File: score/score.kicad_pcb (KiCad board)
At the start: 2 copper layers, 62 x 46 mm, 23 parts, among them J1 Conn_01x02, P8 CONN_01X07, P9 CONN_01X07, U1 74HC595T16-13, U2 HDSP-C8A1, U3 HDSP-C8A1, U4 HDSP-C8A1, U5 74HC595T16-13, U6 74HC595T16-13, U7 TSR1-2433

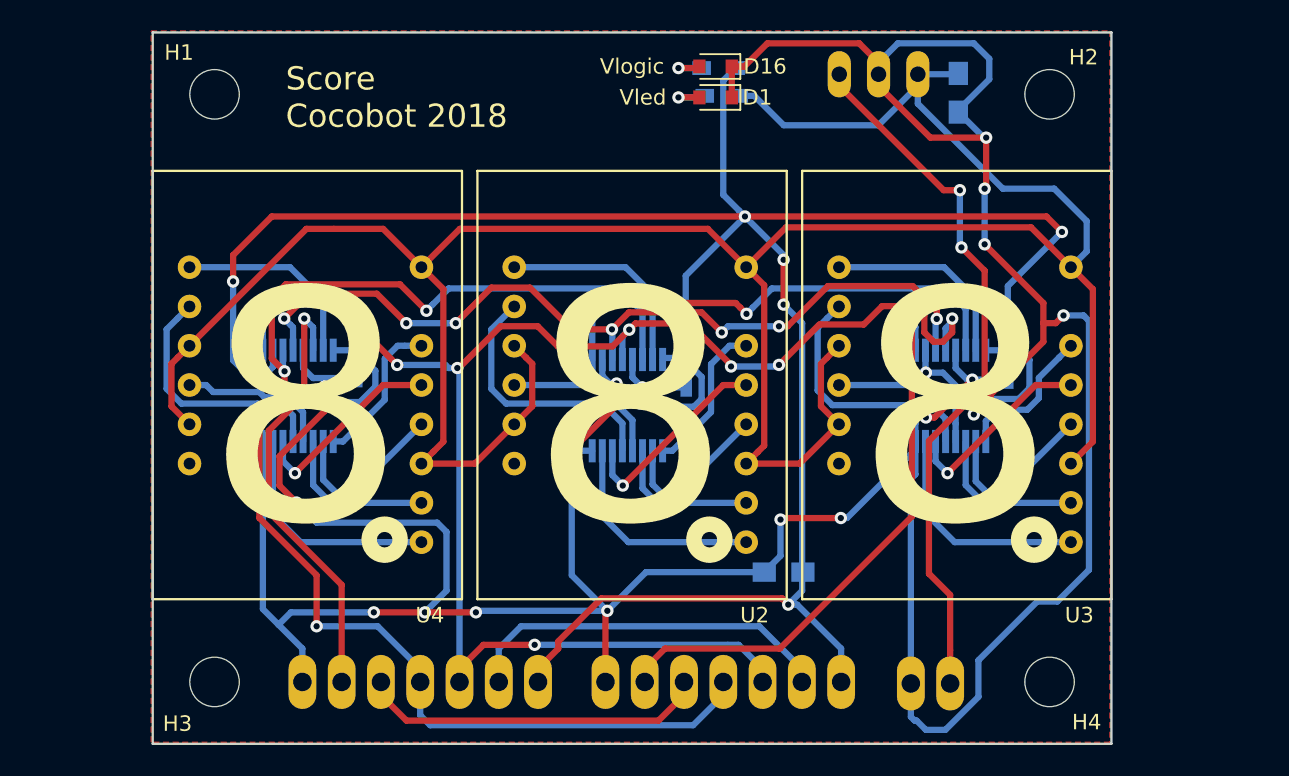
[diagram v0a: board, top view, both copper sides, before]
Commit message: resistor added on 7-seg
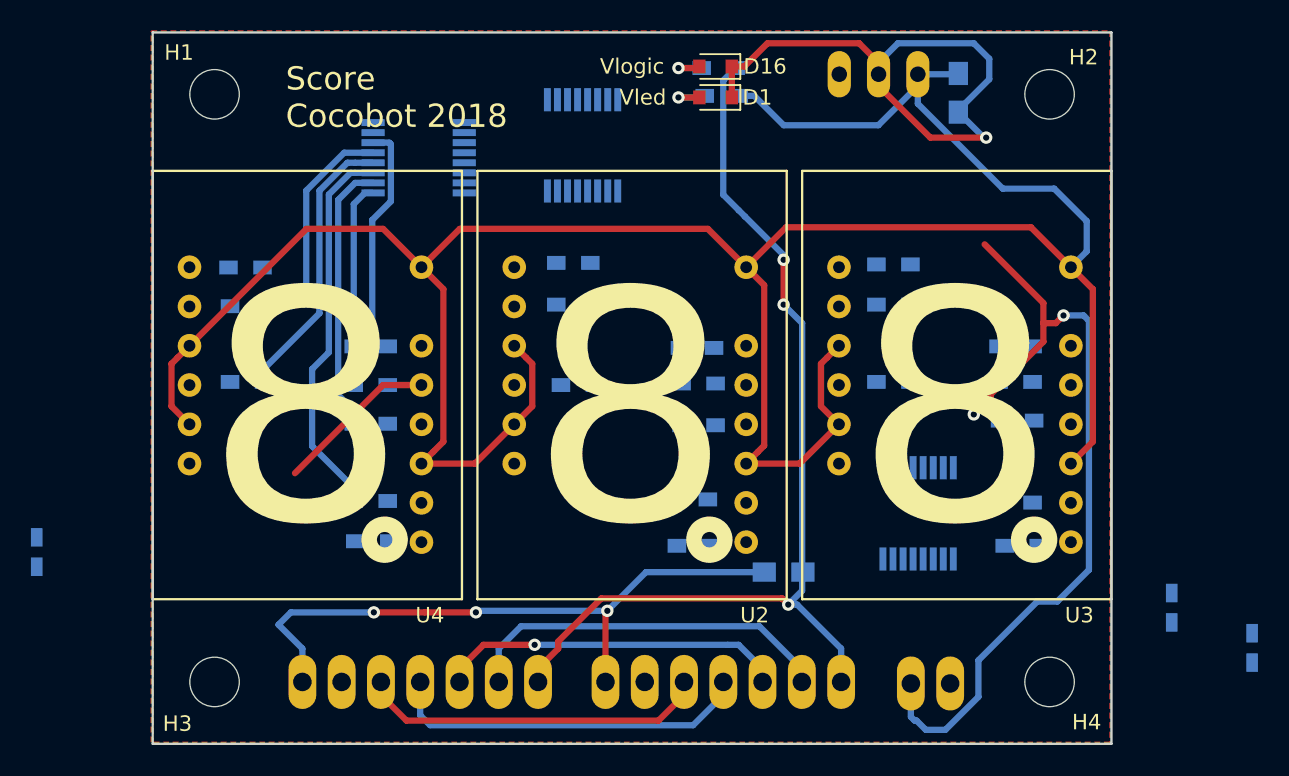
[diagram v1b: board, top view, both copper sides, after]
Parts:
- added R10: 220, espitall:R_0603_HandSoldering, B.Cu at (56.1, 67.7)
- added R11: 220, espitall:R_0603_HandSoldering, B.Cu at (85.2, 70.4)
- added R12: 220, espitall:R_0603_HandSoldering, B.Cu at (77.2, 67.6)
- added R13: 220, espitall:R_0603_HandSoldering, B.Cu at (105.8, 70.3)
- added R14: 220, espitall:R_0603_HandSoldering, B.Cu at (97.9, 67.6)
- added R15: 220, espitall:R_0603_HandSoldering, B.Cu at (85.3, 75.4)
- added R16: 220, espitall:R_0603_HandSoldering, B.Cu at (85.3, 72.7)
- added R17: 220, espitall:R_0603_HandSoldering, B.Cu at (64.1, 75.3)
- added R18: 220, espitall:R_0603_HandSoldering, B.Cu at (64.1, 72.8)
- added R19: 220, espitall:R_0603_HandSoldering, B.Cu at (105.9, 75.1)
- added R20: 220, espitall:R_0603_HandSoldering, B.Cu at (105.8, 72.6)
- added R21: 220, espitall:R_0603_HandSoldering, B.Cu at (84.8, 80.2)
- added R22: 220, espitall:R_0603_HandSoldering, B.Cu at (85.0, 83.2)
- added R23: 220, espitall:R_0603_HandSoldering, B.Cu at (64.1, 80.3)
- added R24: 220, espitall:R_0603_HandSoldering, B.Cu at (64.2, 82.9)
- added R25: 220, espitall:R_0603_HandSoldering, B.Cu at (105.8, 80.4)
- added R26: 220, espitall:R_0603_HandSoldering, B.Cu at (106.2, 83.2)
- added R3: 220, espitall:R_0603_HandSoldering, B.Cu at (56.0, 65.2)
- added R4: 220, espitall:R_0603_HandSoldering, B.Cu at (56.1, 72.6)
- added R5: 220, espitall:R_0603_HandSoldering, B.Cu at (77.2, 64.9)
- added R6: 220, espitall:R_0603_HandSoldering, B.Cu at (77.5, 72.8)
- added R7: 220, espitall:R_0603_HandSoldering, B.Cu at (97.9, 65.0)
- added R8: 220, espitall:R_0603_HandSoldering, B.Cu at (97.9, 72.6)
- added R9: 220, espitall:R_0603_HandSoldering, B.Cu at (64.1, 70.3)
- moved C3 34.9 mm to (115.9, 87.2)
- moved C4 24.2 mm to (121.1, 89.8)
- moved C2 24.0 mm to (42.5, 83.6)
- moved U1 17.3 mm to (67.2, 58.1), turned to 0 degrees
- moved U5 17.0 mm to (77.8, 57.3)
- moved U6 7.88 mm to (99.5, 81.1), turned to 270 degrees
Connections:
- U2 pad 1: /ch8_3v3 -> Net-(R5-Pad1)
- U2 pad 10: /ch11_3v3 -> Net-(R21-Pad1)
- U2 pad 12: /ch10_3v3 -> Net-(R15-Pad1)
- U2 pad 13: /ch14_3v3 -> Net-(R16-Pad1)
- U2 pad 14: /ch9_3v3 -> Net-(R11-Pad1)
- U2 pad 2: /ch13_3v3 -> Net-(R12-Pad1)
- U2 pad 4: /ch12_3v3 -> Net-(R6-Pad1)
- U2 pad 9: /ch15_3v3 -> Net-(R22-Pad1)
- U3 pad 1: /ch16_3v3 -> Net-(R7-Pad1)
- U3 pad 10: /ch19_3v3 -> Net-(R25-Pad1)
- U3 pad 12: /ch18_3v3 -> Net-(R19-Pad1)
- U3 pad 13: /ch22_3v3 -> Net-(R20-Pad1)
- U3 pad 14: /ch17_3v3 -> Net-(R13-Pad1)
- U3 pad 2: /ch21_3v3 -> Net-(R14-Pad1)
- U3 pad 4: /ch20_3v3 -> Net-(R8-Pad1)
- U3 pad 9: /ch23_3v3 -> Net-(R26-Pad1)
- U4 pad 1: /ch0_3v3 -> Net-(R3-Pad1)
- U4 pad 10: /ch3_3v3 -> Net-(R23-Pad1)
- U4 pad 12: /ch2_3v3 -> Net-(R17-Pad1)
- U4 pad 13: /ch6_3v3 -> Net-(R18-Pad1)
- U4 pad 14: /ch1_3v3 -> Net-(R9-Pad1)
- U4 pad 2: /ch5_3v3 -> Net-(R10-Pad1)
- U4 pad 4: /ch4_3v3 -> Net-(R4-Pad1)
- U4 pad 9: /ch7_3v3 -> Net-(R24-Pad1)
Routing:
- net +3V3: track 192.8 -> 66.1 mm, vias 8 -> 3
- net GND: track 249.1 -> 133.4 mm, vias 17 -> 6
- net /sck_3v3: track 110.4 -> 23.7 mm, vias 8 -> 0
- net /set_output_3v3: track 102.8 -> 22.6 mm, vias 8 -> 1
- net Net-(J1-Pad1): track 46.0 -> 0.00 mm, vias 2 -> 0
- net Net-(P9-Pad6): track 36.5 -> 0.00 mm, vias 1 -> 0
- net Net-(U1-Pad9): track 33.1 -> 0.00 mm, vias 2 -> 0
- net Net-(U5-Pad9): track 31.6 -> 0.00 mm, vias 2 -> 0
- net /mosi_3v3: track 28.7 -> 0.00 mm, vias 1 -> 0
- net /ch13_3v3: track 17.1 -> 0.00 mm
- net /ch21_3v3: track 16.5 -> 0.00 mm
- net /ch7_3v3: track 15.1 -> 0.00 mm
- net /ch23_3v3: track 14.8 -> 0.00 mm
- net /ch3_3v3: track 10.3 -> 24.8 mm
- net /ch15_3v3: track 14.2 -> 0.00 mm
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
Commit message: score board routed
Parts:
- moved C3 39.1 mm to (86.9, 61.0)
- moved C2 32.4 mm to (65.3, 60.6)
- moved C4 31.7 mm to (106.8, 61.5)
- moved U6 17.5 mm to (101.7, 63.8), turned to 90 degrees
- moved U1 8.47 mm to (60.2, 62.9), turned to 90 degrees
- moved U5 6.95 mm to (81.8, 63.0)
- moved R1 5.91 mm to (80.7, 52.3), turned to 0 degrees
- moved C1 5.88 mm to (96.0, 87.6), turned to 0 degrees
- moved R3 3.71 mm to (53.5, 62.5)
- moved R7 3.39 mm to (95.4, 62.7)
- moved R5 3.34 mm to (74.5, 62.9)
- moved R14 2.74 mm to (98.7, 70.2)
- moved R12 2.68 mm to (77.7, 70.2)
- moved R10 2.53 mm to (56.9, 70.1)
- moved R8 0.80 mm to (98.7, 72.8)
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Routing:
- net /sck_3v3: track 23.7 -> 120.8 mm, vias 0 -> 6
- net /set_output_3v3: track 22.6 -> 114.9 mm, vias 1 -> 7
- net +3V3: track 66.1 -> 136.3 mm, vias 3 -> 8
- net Net-(P9-Pad6): track 0.00 -> 51.3 mm
- net Net-(J1-Pad1): track 0.00 -> 48.5 mm, vias 0 -> 1
- net /mosi_3v3: track 0.00 -> 47.3 mm
- net Net-(U1-Pad9): track 0.00 -> 30.6 mm, vias 0 -> 2
- net GND: track 133.4 -> 105.1 mm, vias 6 -> 10
- net Net-(U5-Pad9): track 0.00 -> 27.4 mm, vias 0 -> 2
- net /ch19_3v3: track 0.00 -> 26.1 mm
- net /ch15_3v3: track 0.00 -> 24.7 mm
- net /ch7_3v3: track 0.00 -> 22.0 mm
- net /ch23_3v3: track 0.00 -> 22.0 mm
- net /ch22_3v3: track 0.00 -> 19.8 mm
- net +3.3VP: track 175.2 -> 157.2 mm
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
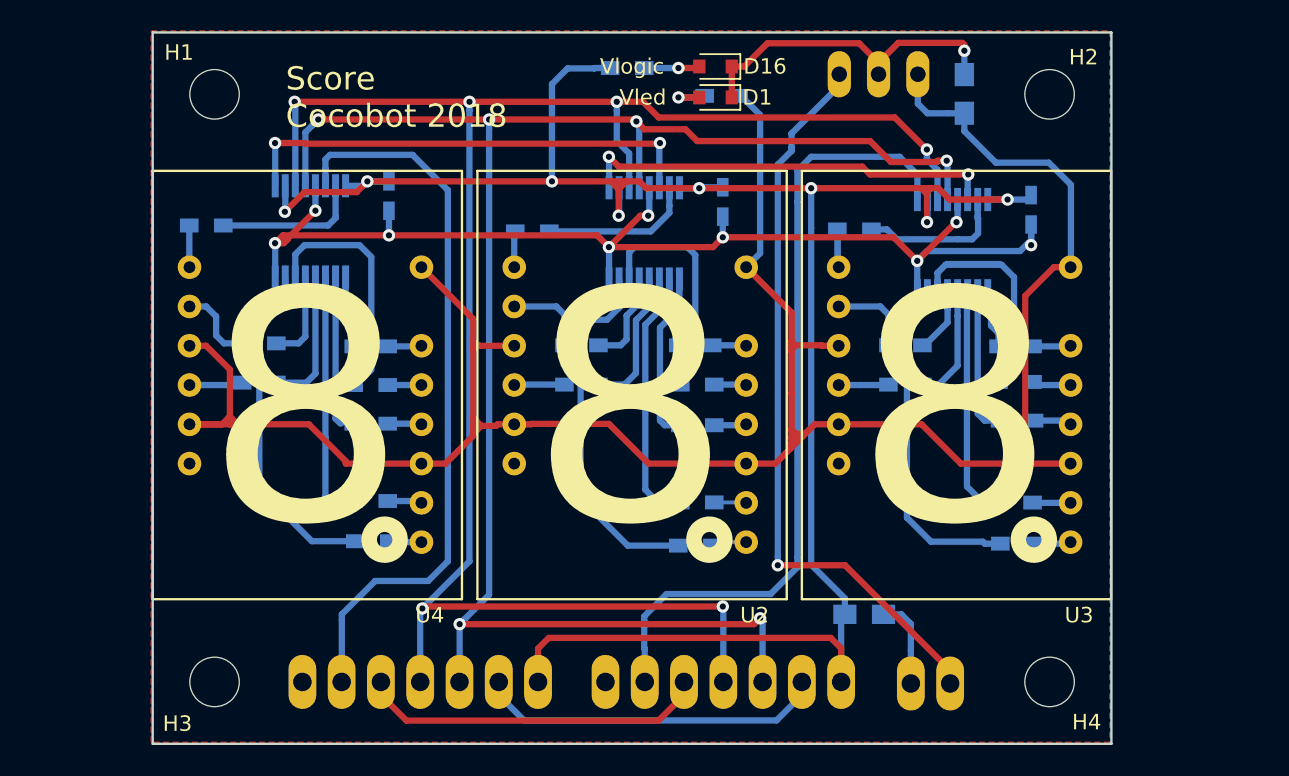
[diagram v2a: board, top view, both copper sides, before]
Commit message: rerouting for non metalized holes
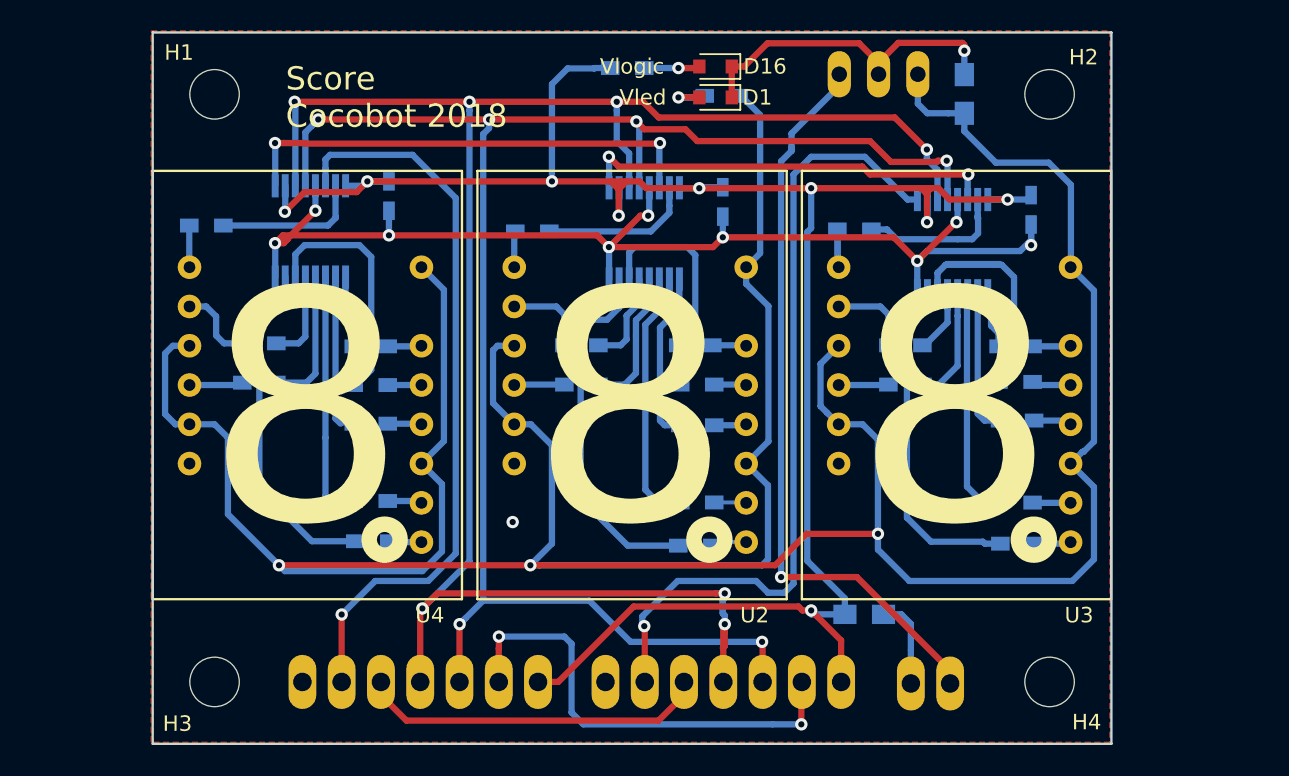
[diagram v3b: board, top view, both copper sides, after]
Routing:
- net +3.3VP: track 157.2 -> 229.8 mm, vias 0 -> 3
- net /load_input_3v3: track 22.7 -> 31.9 mm, vias 0 -> 2
- net /sck_3v3: track 120.8 -> 125.1 mm, vias 6 -> 7
- net /set_output_3v3: track 114.9 -> 112.8 mm
- net /mosi_3v3: track 47.3 -> 48.6 mm, vias 0 -> 1
- net +3V3: track 136.3 -> 135.5 mm, vias 8 -> 9
- net Net-(P9-Pad6): track 51.3 -> 51.8 mm, vias 0 -> 1
- net GND: vias 10 -> 11

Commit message: rerouting for non metalized holes...2
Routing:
- net GND: track 105.1 -> 115.2 mm, vias 11 -> 14
- net Net-(J1-Pad1): track 48.6 -> 50.6 mm
- net +3V3: track 135.5 -> 137.2 mm
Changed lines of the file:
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@@
     (thickness 1.6)
     (drawings 11)
-    (tracks 593)
+    (tracks 602)
     (zones 0)
     (modules 47)
@@
   (page A4)
   (layers
-    (0 F.Cu signal)
+    (0 F.Cu signal hide)
     (31 B.Cu signal)
     (32 B.Adhes user)
@@
   )
   (setup
-    (last_trace_width 0.4064)
+    (last_trace_width 0.25)
     (user_trace_width 0.254)
     (user_trace_width 0.4064)
@@
   (gr_line (start 50 96) (end 112 96) (layer Edge.Cuts) (width 0.15))
   (gr_line (start 50 50) (end 112 50) (layer Edge.Cuts) (width 0.15))
-  (segment (start 76.22683 92) (end 81.10483 87.122) (width 0.4064) (layer F.Cu) (net 1))
-  (segment (start 74.92 92) (end 76.22683 92) (width 0.4064) (layer F.Cu) (net 1))
-  (segment (start 81.10483 87.122) (end 91.763315 87.122) (width 0.4064) (layer F.Cu) (net 1))
+  (segment (start 74.92 89.164) (end 76.962 87.122) (width 0.4064) (layer F.Cu) (net 1))
+  (segment (start 74.92 92) (end 74.92 89.164) (width 0.4064) (layer F.Cu) (net 1))
+  (segment (start 76.962 87.122) (end 91.763315 87.122) (width 0.4064) (layer F.Cu) (net 1))
   (segment (start 91.763315 87.122) (end 92.017315 87.376) (width 0.4064) (layer F.Cu) (net 1))
   (segment (start 92.017315 87.376) (end 92.583 87.376) (width 0.4064) (layer F.Cu) (net 1))
@@
   (segment (start 58.573 59.915) (end 58.573 61.569) (width 0.4064) (layer B.Cu) (net 1))
   (via (at 58.547 61.595) (size 0.8) (drill 0.4) (layers F.Cu B.Cu) (net 1))
+  (via (at 59.68 88.402) (size 0.8) (drill 0.4) (layers F.Cu B.Cu) (net 2))
+  (segment (start 59.68 92) (end 59.68 88.402) (width 0.25) (layer F.Cu) (net 2))
+  (via (at 79.28 89.313) (size 0.8) (drill 0.4) (layers F.Cu B.Cu) (net 2))
+  (segment (start 79.28 92) (end 79.28 89.313) (width 0.25) (layer F.Cu) (net 2))
+  (segment (start 99.06 88.2716) (end 99.03 88.2416) (width 0.25) (layer F.Cu) (net 2))
+  (segment (start 99.06 90.06994) (end 99.06 88.2716) (width 0.25) (layer F.Cu) (net 2))
+  (via (at 99.03 88.2416) (size 0.8) (drill 0.4) (layers F.Cu B.Cu) (net 2))
+  (segment (start 99.03 92.1) (end 99.03 90.09994) (width 0.25) (layer F.Cu) (net 2))
+  (segment (start 99.03 90.09994) (end 99.06 90.06994) (width 0.25) (layer F.Cu) (net 2))
   (via (at 73.279 81.661) (size 0.8) (drill 0.4) (layers F.Cu B.Cu) (net 2))
   (segment (start 97.262 87.63) (end 98.4184 87.63) (width 0.4064) (layer B.Cu) (net 2))
@@
   (segment (start 104.700001 70.3) (end 104.700001 69.4436) (width 0.4064) (layer B.Cu) (net 37))
   (segment (start 104.700001 69.4436) (end 104.217401 68.961) (width 0.4064) (layer B.Cu) (net 37))
-  (segment (start 101.57 91.25037) (end 95.53663 85.217) (width 0.4064) (layer F.Cu) (net 38))
+  (segment (start 101.57 87.854) (end 98.933 85.217) (width 0.4064) (layer F.Cu) (net 38))
+  (segment (start 101.57 92.1) (end 101.57 87.854) (width 0.4064) (layer F.Cu) (net 38))
+  (segment (start 98.933 85.217) (end 91.202475 85.217) (width 0.4064) (layer F.Cu) (net 38))
+  (segment (start 91.202475 85.217) (end 90.63679 85.217) (width 0.4064) (layer F.Cu) (net 38))
   (via (at 90.63679 85.217) (size 0.8) (drill 0.4) (layers F.Cu B.Cu) (net 38))
   (segment (start 91.313 57.658) (end 90.63679 58.33421) (width 0.4064) (layer B.Cu) (net 38))
-  (segment (start 91.202475 85.217) (end 90.63679 85.217) (width 0.4064) (layer F.Cu) (net 38))
-  (segment (start 95.53663 85.217) (end 91.202475 85.217) (width 0.4064) (layer F.Cu) (net 38))
   (segment (start 90.63679 84.651315) (end 90.63679 85.217) (width 0.4064) (layer B.Cu) (net 38))
-  (segment (start 101.57 92.1) (end 101.57 91.25037) (width 0.4064) (layer F.Cu) (net 38))
   (segment (start 90.63679 58.33421) (end 90.63679 84.651315) (width 0.4064) (layer B.Cu) (net 38))
   (segment (start 91.313 57.658) (end 91.313 57.404) (width 0.4064) (layer B.Cu) (net 38))

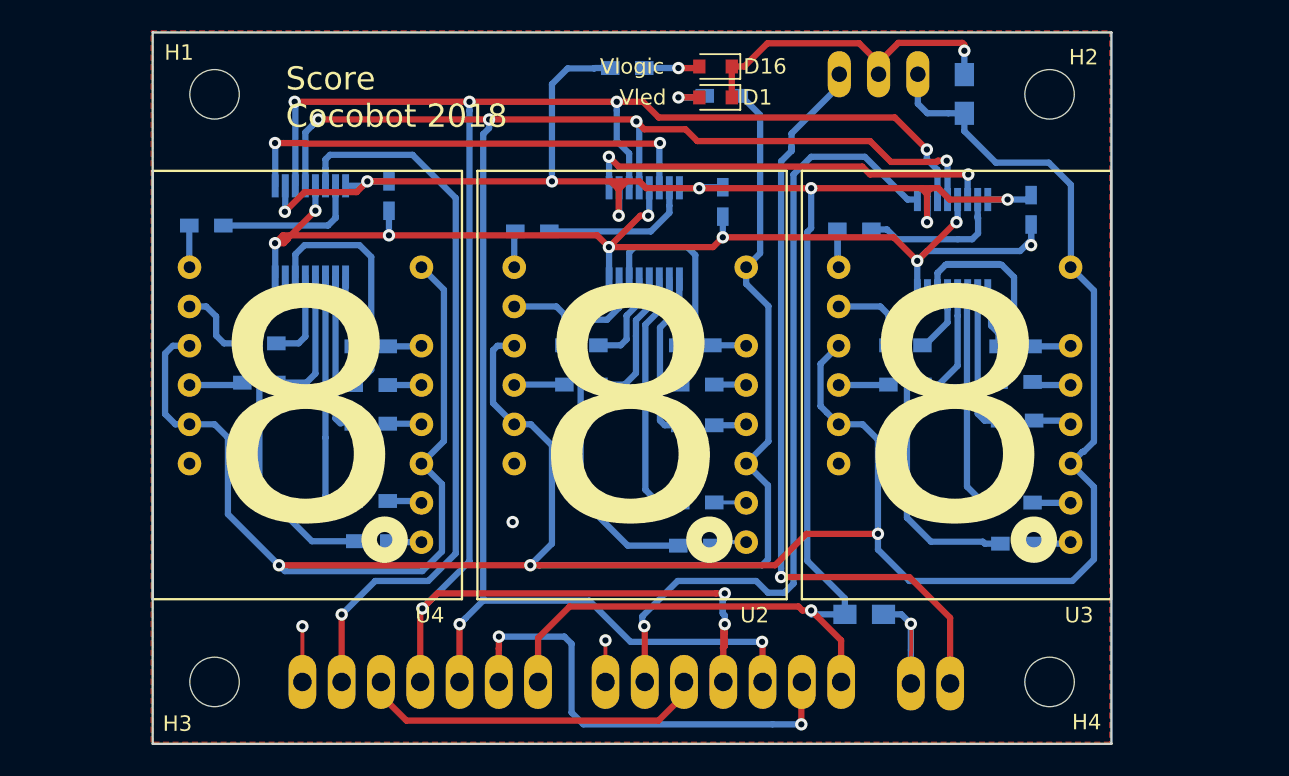
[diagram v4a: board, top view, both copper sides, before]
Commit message: modified via diameter
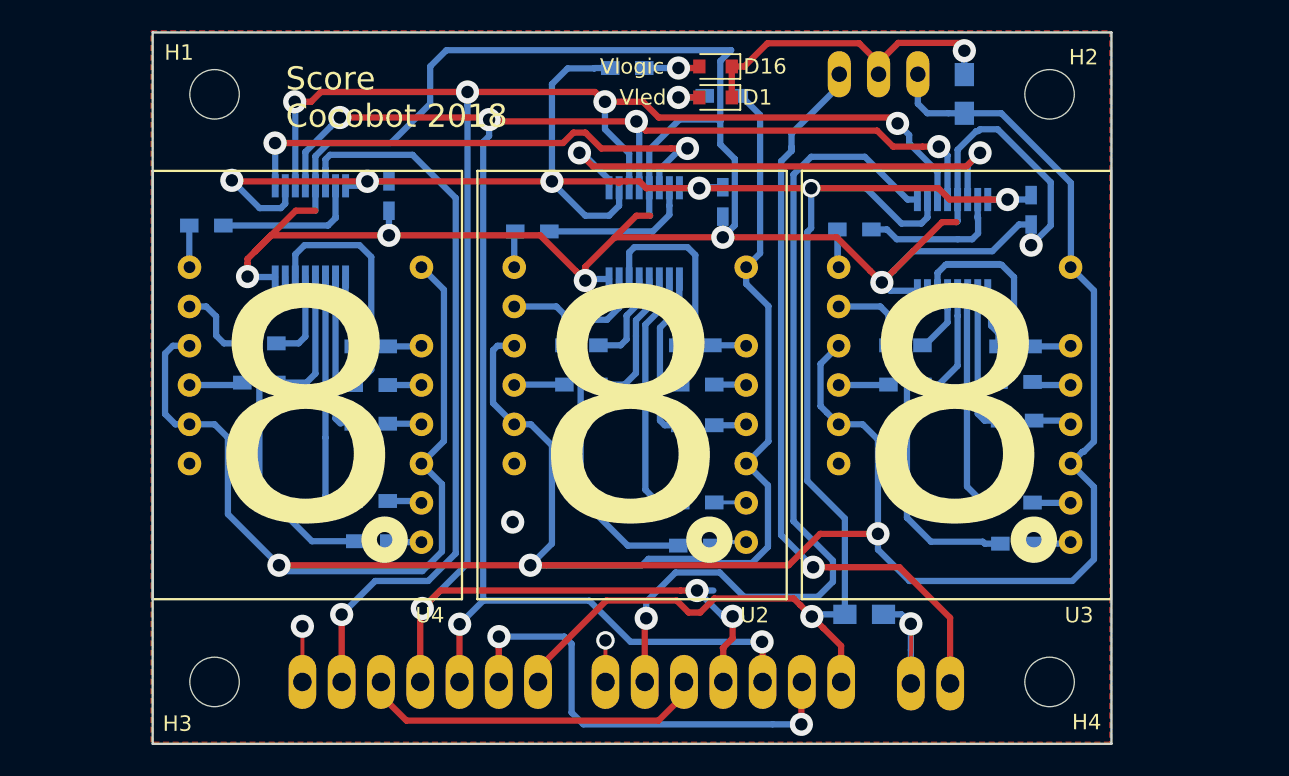
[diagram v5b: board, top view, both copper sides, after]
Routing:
- net GND: track 115.2 -> 194.9 mm, vias 14 -> 11
- net +3V3: track 137.2 -> 149.8 mm, vias 9 -> 7
- net Net-(U5-Pad9): track 27.4 -> 33.1 mm
- net Net-(P9-Pad6): track 51.8 -> 56.2 mm
- net Net-(U1-Pad9): track 30.6 -> 33.7 mm
- net Net-(J1-Pad1): track 50.6 -> 49.0 mm
- net +3.3VP: track 229.8 -> 228.9 mm
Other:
- net class Default: via_dia 0.8 -> 1.5; via_drill 0.4 -> 0.8
- rule via_min_drill: 0.3 -> 0.8
- rule via_min_size: 0.4 -> 0.8
